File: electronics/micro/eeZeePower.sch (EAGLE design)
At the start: 10 parts

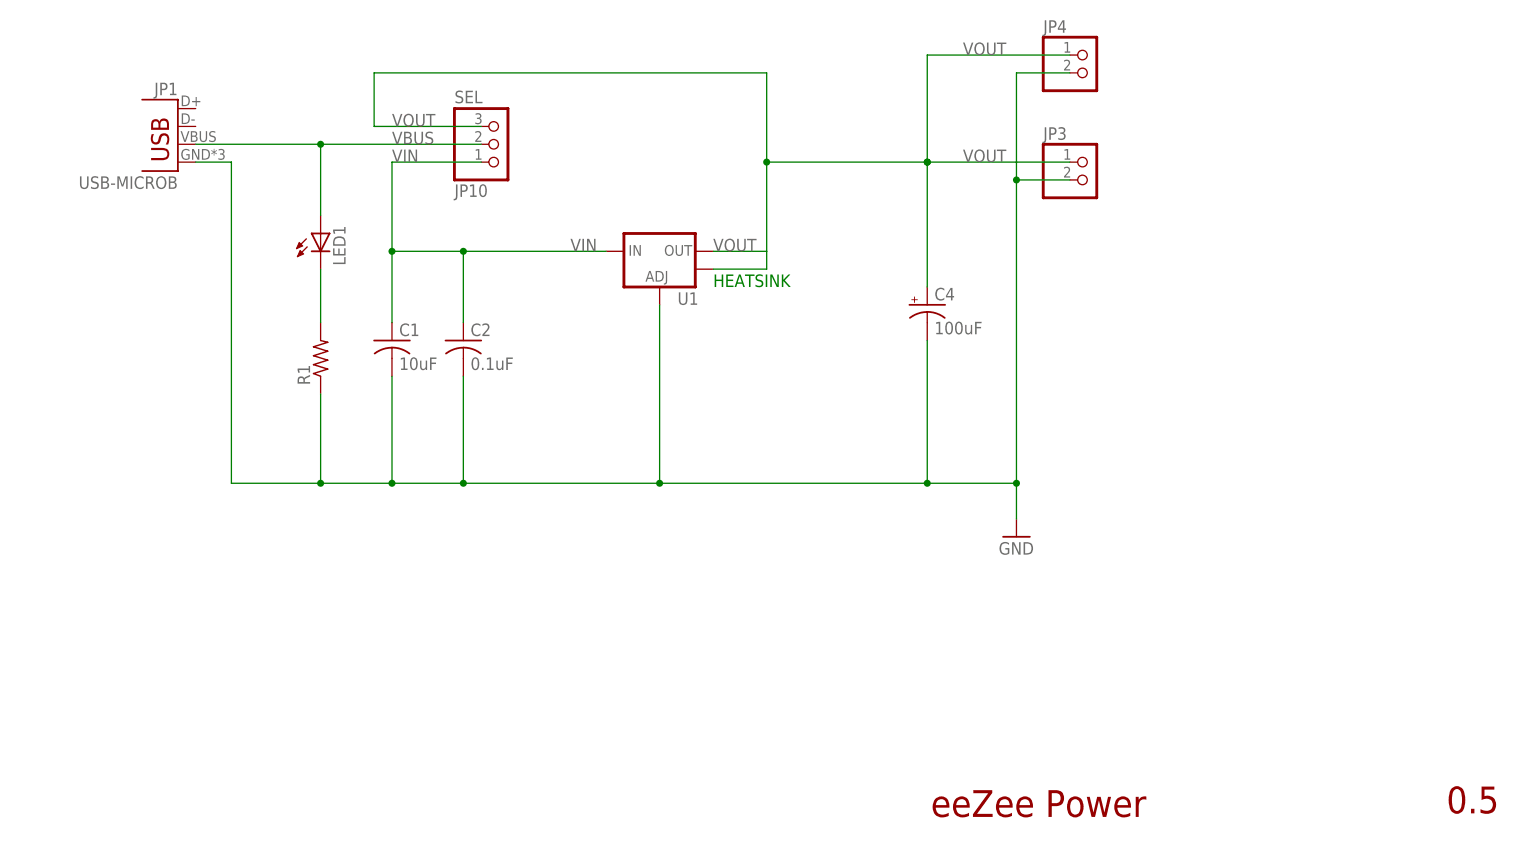
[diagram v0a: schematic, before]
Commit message: updated microb with new four-pad library version, added shielding to ground, fixed missing junction
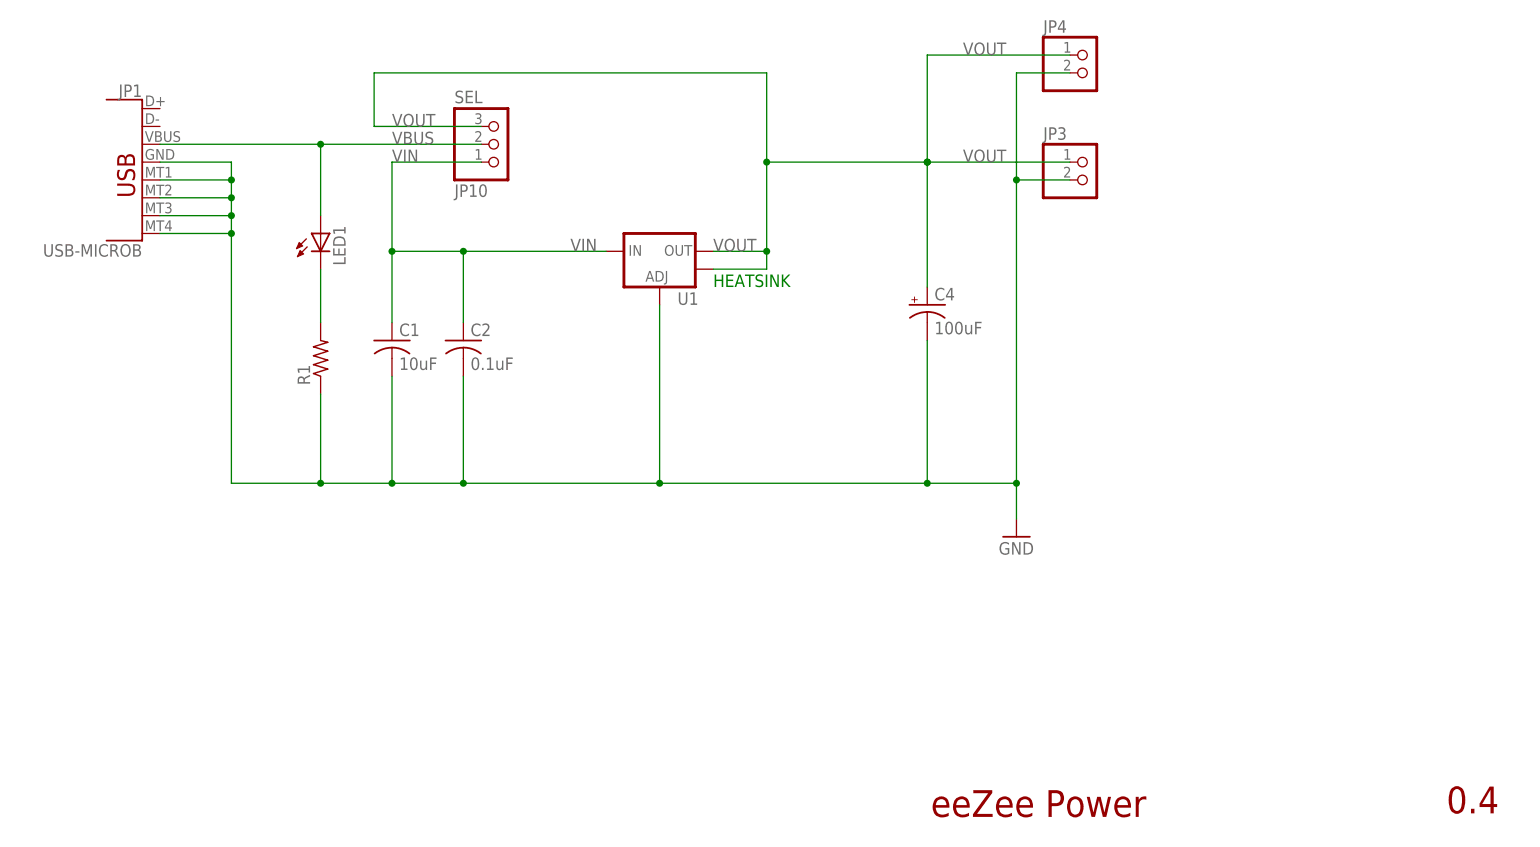
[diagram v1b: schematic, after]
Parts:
- JP1: device SparkFun-Connectors:USB-MICROB -> bt_electromech:USB-MICROB
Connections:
- net GND: now also JP1.SHIELD1, JP1.SHIELD2, JP1.SHIELD3, JP1.SHIELD4
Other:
- note added: "0.4"
- note removed: "0.5"
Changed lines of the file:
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@@
 <part name="JP3" library="pinhead-2" deviceset="PINHD-1X02" device="_2.54-S"/>
 <part name="JP4" library="pinhead-2" deviceset="PINHD-1X02" device="_2.54-S"/>
-<part name="JP1" library="SparkFun-Connectors" deviceset="USB" device="-MICROB"/>
+<part name="JP1" library="bt_electromech" deviceset="USB" device="-MICROB"/>
 </parts>
 <sheets>
@@
 <plain>
 <text x="160.528" y="23.622" size="3.81" layer="94">eeZee Power</text>
-<text x="233.934" y="24.13" size="3.81" layer="94">0.5</text>
+<text x="233.934" y="24.13" size="3.81" layer="94">0.4</text>
 <text x="129.54" y="99.06" size="1.778" layer="91">HEATSINK</text>
 </plain>
@@
 <instance part="JP3" gate="A" x="182.88" y="114.3"/>
 <instance part="JP4" gate="A" x="182.88" y="129.54"/>
-<instance part="JP1" gate="G$1" x="53.34" y="116.84" rot="MR0"/>
+<instance part="JP1" gate="G$1" x="48.26" y="116.84" rot="MR0"/>
 </instances>
 <busses>
@@
 <wire x1="83.82" y1="71.12" x2="83.82" y2="86.36" width="0.1524" layer="91"/>
 <junction x="93.98" y="71.12"/>
-<wire x1="60.96" y1="71.12" x2="60.96" y2="116.84" width="0.1524" layer="91"/>
+<wire x1="60.96" y1="71.12" x2="60.96" y2="106.68" width="0.1524" layer="91"/>
+<wire x1="60.96" y1="106.68" x2="60.96" y2="109.22" width="0.1524" layer="91"/>
+<wire x1="60.96" y1="109.22" x2="60.96" y2="111.76" width="0.1524" layer="91"/>
+<wire x1="60.96" y1="111.76" x2="60.96" y2="114.3" width="0.1524" layer="91"/>
+<wire x1="60.96" y1="114.3" x2="60.96" y2="116.84" width="0.1524" layer="91"/>
 <wire x1="83.82" y1="71.12" x2="73.66" y2="71.12" width="0.1524" layer="91"/>
 <pinref part="R1" gate="G$1" pin="1"/>
@@
 <wire x1="121.92" y1="71.12" x2="160.02" y2="71.12" width="0.1524" layer="91"/>
 <pinref part="JP1" gate="G$1" pin="GND"/>
-<wire x1="55.88" y1="116.84" x2="60.96" y2="116.84" width="0.1524" layer="91"/>
+<wire x1="50.8" y1="116.84" x2="60.96" y2="116.84" width="0.1524" layer="91"/>
+<pinref part="JP1" gate="G$1" pin="SHIELD2"/>
+<wire x1="50.8" y1="111.76" x2="60.96" y2="111.76" width="0.1524" layer="91"/>
+<junction x="60.96" y="111.76"/>
+<pinref part="JP1" gate="G$1" pin="SHIELD3"/>
+<wire x1="50.8" y1="109.22" x2="60.96" y2="109.22" width="0.1524" layer="91"/>
+<junction x="60.96" y="109.22"/>
+<pinref part="JP1" gate="G$1" pin="SHIELD4"/>
+<wire x1="50.8" y1="106.68" x2="60.96" y2="106.68" width="0.1524" layer="91"/>
+<junction x="60.96" y="106.68"/>
+<pinref part="JP1" gate="G$1" pin="SHIELD1"/>
+<wire x1="50.8" y1="114.3" x2="60.96" y2="114.3" width="0.1524" layer="91"/>
+<junction x="60.96" y="114.3"/>
 </segment>
 </net>
@@
 <pinref part="U1" gate="G$1" pin="OUT@1"/>
 <wire x1="129.54" y1="101.6" x2="137.16" y2="101.6" width="0.1524" layer="91"/>
+<junction x="137.16" y="104.14"/>
 </segment>
 </net>
@@
 <label x="83.82" y="119.38" size="1.778" layer="95"/>
 <pinref part="JP1" gate="G$1" pin="VBUS"/>
-<wire x1="55.88" y1="119.38" x2="73.66" y2="119.38" width="0.1524" layer="91"/>
+<wire x1="50.8" y1="119.38" x2="73.66" y2="119.38" width="0.1524" layer="91"/>
 </segment>
 </net>
